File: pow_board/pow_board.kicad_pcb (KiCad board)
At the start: 2 copper layers, 62 x 89.4 mm, 17 parts, among them J1 POWER IN, J2 EXT_USB, J3 EXT_BAT, SW1 SW_SPST, U1 Battery charger module, U2 Step-up DC-DC, U3 Step-down DC-DC

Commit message: Fixed modules sizes
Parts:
- moved U1 0.39 mm to (51.5, 91.6)
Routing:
- net Net-(SW1-B): track 27.5 -> 26.0 mm
- net +BATT: track 87.0 -> 88.5 mm
- net Net-(SW1-A): track 19.5 -> 18.0 mm
- net +5V: track 42.8 -> 43.9 mm
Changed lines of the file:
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@@
 		(at 101.33 82.796 180)
 		(property "Reference" "U2"
-			(at 0.04 13.59 180)
+			(at 16.92 13.56 180)
 			(unlocked yes)
 			(layer "F.SilkS")
@@
 		)
 		(property "Value" "Step-up DC-DC"
-			(at 10.667 22.08 180)
+			(at 16.92 15.06 180)
 			(unlocked yes)
 			(layer "F.Fab")
@@
 		)
 		(property "Footprint" "0a_pow:MT3608_step-up_DC-DC"
-			(at 0.04 14.09 180)
+			(at 16.92 14.06 180)
 			(unlocked yes)
 			(layer "F.Fab")
@@
 		)
 		(property "Datasheet" ""
-			(at 0.04 14.09 180)
+			(at 16.92 14.06 180)
 			(unlocked yes)
 			(layer "F.Fab")
@@
 		)
 		(property "Description" "https://www.mini-tech.com.ua/dc-dc-konverter-povyshayushchij-mt3608"
-			(at 0.04 14.09 180)
+			(at 16.92 14.06 180)
 			(unlocked yes)
 			(layer "F.Fab")
@@
 			)
 		)
-		(sheetname "Root")
-		(sheetfile "pow_board.kicad_sch")
 		(attr through_hole)
 		(fp_rect
-			(start -3.1355 -4.74)
-			(end 34.0755 12.532)
+			(start -3.01 -5.03)
+			(end 32.99 11.97)
 			(stroke
 				(width 0.05)
@@
 			(layer "F.SilkS")
 		)
-		(fp_rect
-			(start -3.1355 -4.74)
-			(end 34.0755 12.532)
-			(stroke
-				(width 0.05)
-				(type default)
-			)
-			(fill none)
-			(layer "F.CrtYd")
-		)
 		(fp_text user "${REFERENCE}"
-			(at 0.04 16.59 180)
+			(at 16.92 16.56 180)
 			(unlocked yes)
 			(layer "F.Fab")
@@
 		)
 		(pad "1" thru_hole rect
-			(at 0 7.87417 180)
+			(at 0 6.5 180)
 			(size 1.7 1.7)
 			(drill 1)
@@
 		)
 		(pad "3" thru_hole rect
-			(at 31.5 0 180)
+			(at 30.5 0 180)
 			(size 1.7 1.7)
 			(drill 1)
@@
 		)
 		(pad "4" thru_hole rect
-			(at 31.5 7.87417 180)
+			(at 30.5 6.5 180)
 			(size 1.7 1.7)
 			(drill 1)
@@
 			(at 4.385 4.81 180)
 			(layer "F.Fab")
+			(hide yes)
 			(effects
 				(font
@@
 			(at 4.385 4.81 0)
 			(layer "F.Fab")
+			(hide yes)
 			(effects
 				(font
@@
 			(at 4.385 12.43 180)
 			(layer "F.Fab")
+			(hide yes)
 			(effects
 				(font
@@
 			(unlocked yes)
 			(layer "F.Fab")
+			(hide yes)
 			(effects
 				(font
@@
 			(at 4.385 4.81 -90)
 			(layer "F.Fab")
+			(hide yes)
 			(effects
 				(font
@@
 	(footprint "0a_pow:TP4056_module_typeC"
 		(layer "F.Cu")
-		(at 51.27 91.3)
+		(at 51.48 91.63)
 		(property "Reference" "U1"
 			(at 0.31 -12.61 0)
@@
 		)
 		(property "Value" "Battery charger module"
-			(at 16.7905 -11.094 0)
+			(at 0.31 -11.11 0)
 			(unlocked yes)
 			(layer "F.Fab")
+			(hide yes)
 			(effects
 				(font
@@
 			)
 		)
-		(sheetname "Root")
-		(sheetfile "pow_board.kicad_sch")
 		(attr through_hole)
 		(fp_rect
-			(start -1.79 3.76)
-			(end 2.67 9.97)
+			(start -2.2 3.755)
+			(end 2.26 9.965)
 			(stroke
 				(width 0.1)
@@
 		)
 		(fp_rect
-			(start -1.21 -1.41)
-			(end 25.79 15.59)
+			(start -1.73 -1.57)
+			(end 26.27 15.63)
 			(stroke
 				(width 0.05)
@@
 			(layer "F.SilkS")
 		)
-		(fp_rect
-			(start -1.21 -1.41)
-			(end 25.79 15.59)
-			(stroke
-				(width 0.05)
-				(type default)
-			)
-			(fill none)
-			(layer "F.CrtYd")
-		)
 		(fp_text user "${REFERENCE}"
 			(at 0.31 -9.61 0)
@@
 		)
 		(pad "3" thru_hole rect
-			(at 22 0)
+			(at 23 0)
 			(size 1.7 1.7)
 			(drill 1)
@@
 		)
 		(pad "4" thru_hole rect
-			(at 22 14)
+			(at 23 14)
 			(size 1.7 1.7)
 			(drill 1)
@@
 		)
 		(pad "5" thru_hole rect
-			(at 22 3)
+			(at 23 2.54)
 			(size 1.7 1.7)
 			(drill 1)
@@
 		)
 		(pad "6" thru_hole rect
-			(at 22 11)
+			(at 23 11.46)
 			(size 1.7 1.7)
 			(drill 1)
@@
 			(at 0 -1.85 180)
 			(layer "B.Fab")
+			(hide yes)
 			(effects
 				(font
@@
 			(at 0.6 -11.3325 90)
 			(layer "B.Fab")
+			(hide yes)
 			(effects
 				(font
@@
 			(at 0 -1.85 180)
 			(layer "B.Fab")
+			(hide yes)
 			(effects
 				(font
@@
 			(at 0 -1.82 0)
 			(layer "B.Fab")
+			(hide yes)
 			(effects
 				(font
@@
 			(at 0 -1.85 -90)
 			(layer "B.Fab")
+			(hide yes)
 			(effects
 				(font
@@
 			(at 0 -1.85 -90)
 			(layer "B.Fab")
+			(hide yes)
 			(effects
 				(font
@@
 	)
 	(gr_text "U"
-		(at 52.33 114.01 180)
+		(at 52.54 114.56 180)
 		(layer "B.Cu")
 		(effects
@@
 	)
 	(gr_text "G"
-		(at 52.32 116.41 180)
+		(at 52.53 116.96 180)
 		(layer "B.Cu")
 		(effects
@@
 	)
 	(segment
-		(start 87.13 62.05)
-		(end 87.13 73.39)
+		(start 56.91 71.51)
+		(end 56.11 71.51)
 		(width 1)
 		(layer "B.Cu")
@@
 	)
 	(segment
-		(start 56.91 71.51)
-		(end 56.11 71.51)
+		(start 86.4 61.41)
+		(end 73.69 61.41)
 		(width 1)
 		(layer "B.Cu")
@@
 	)
 	(segment
-		(start 70.58 94.34)
-		(end 73.12 94.34)
+		(start 59.46 66.27)
+		(end 59.46 71.39)
 		(width 1)
 		(layer "B.Cu")
@@
 	)
 	(segment
-		(start 73.03 94.01)
-		(end 73.05 93.99)
+		(start 59.46 71.39)
+		(end 59.58 71.51)
 		(width 1)
 		(layer "B.Cu")
@@
 	)
 	(segment
-		(start 86.4 61.41)
-		(end 73.69 61.41)
+		(start 87.13 73.39)
+		(end 69.63 90.89)
 		(width 1)
 		(layer "B.Cu")
@@
 	)
 	(segment
-		(start 87.13 73.39)
-		(end 69.63 90.89)
+		(start 73.69 61.41)
+		(end 63.59 71.51)
 		(width 1)
 		(layer "B.Cu")
@@
 	)
 	(segment
-		(start 59.46 66.27)
-		(end 59.46 71.39)
+		(start 69.63 93.39)
+		(end 70.32 94.08)
 		(width 1)
 		(layer "B.Cu")
@@
 	)
 	(segment
-		(start 59.46 71.39)
-		(end 59.58 71.51)
+		(start 55.32 72.3)
+		(end 55.32 75.95)
 		(width 1)
 		(layer "B.Cu")
@@
 	)
 	(segment
-		(start 69.63 93.39)
-		(end 70.58 94.34)
+		(start 63.59 71.51)
+		(end 59.58 71.51)
 		(width 1)
 		(layer "B.Cu")
@@
 	)
 	(segment
-		(start 73.69 61.41)
-		(end 63.59 71.51)
+		(start 55.32 75.95)
+		(end 55.33 75.96)
 		(width 1)
 		(layer "B.Cu")
@@
 	)
 	(segment
-		(start 55.32 72.3)
-		(end 55.32 75.95)
+		(start 70.32 94.08)
+		(end 74.73 94.08)
 		(width 1)
 		(layer "B.Cu")
@@
 	)
 	(segment
-		(start 63.59 71.51)
-		(end 59.58 71.51)
+		(start 87.13 62.05)
+		(end 87.13 73.39)
 		(width 1)
 		(layer "B.Cu")
@@
 	)
 	(segment
-		(start 55.32 75.95)
-		(end 55.33 75.96)
+		(start 59.046 82.796)
+		(end 59.02 82.77)
 		(width 1)
 		(layer "B.Cu")
-		(net 2)
+		(net 3)
 	)
 	(segment
@@
 	)
 	(segment
-		(start 59.046 82.796)
-		(end 59.02 82.77)
+		(start 70.86 82.73)
+		(end 70.794 82.796)
 		(width 1)
 		(layer "B.Cu")
@@
 	)
 	(segment
-		(start 69.83 82.796)
+		(start 70.794 82.796)
 		(end 59.046 82.796)
 		(width 1)
@@
 	)
 	(segment
-		(start 82.29 91.06)
-		(end 73.28 91.06)
+		(start 74.53 91.65)
+		(end 74.46 91.58)
 		(width 1)
 		(layer "B.Cu")
@@
 	)
 	(segment
-		(start 73.28 91.06)
-		(end 73.18 91.16)
+		(start 85.765 94.535)
+		(end 82.88 91.65)
 		(width 1)
 		(layer "B.Cu")
@@
 	)
 	(segment
-		(start 85.765 94.535)
-		(end 82.29 91.06)
+		(start 82.88 91.65)
+		(end 74.53 91.65)
 		(width 1)
 		(layer "B.Cu")
@@
 	)
 	(segment
-		(start 103.37 76.96)
-		(end 103.37 87.89)
+		(start 99.39 91.87)
+		(end 99.39 91.89)
 		(width 1)
 		(layer "B.Cu")
@@
 	)
 	(segment
-		(start 101.3 74.89)
-		(end 103.37 76.96)
+		(start 103.16 78.05)
+		(end 103.16 88.1)
 		(width 1)
 		(layer "B.Cu")
@@
 	)
 	(segment
-		(start 99.39 91.87)
-		(end 99.39 91.89)
+		(start 103.16 88.1)
+		(end 99.39 91.87)
 		(width 1)
 		(layer "B.Cu")
@@
 	)
 	(segment
-		(start 103.37 87.89)
-		(end 99.39 91.87)
+		(start 101.3 76.19)
+		(end 103.16 78.05)
 		(width 1)
 		(layer "B.Cu")

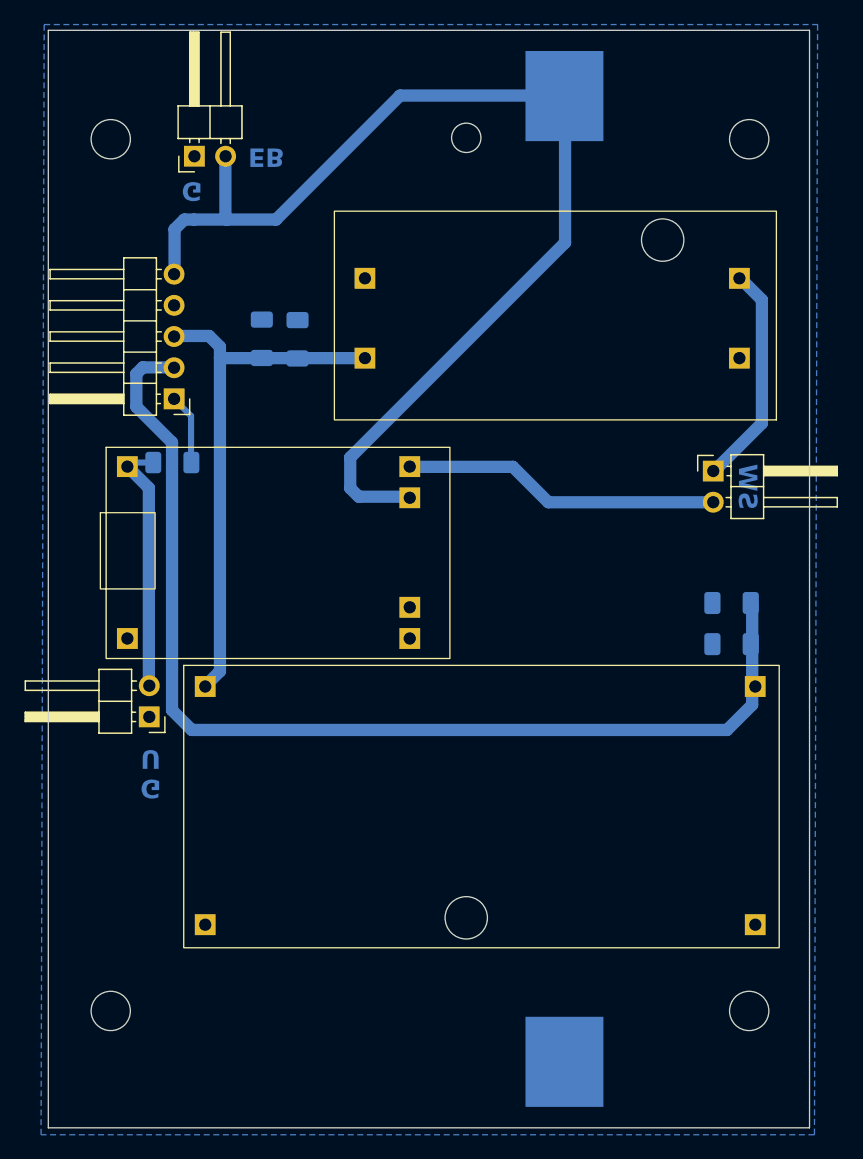
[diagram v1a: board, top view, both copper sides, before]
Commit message: Recovering after git fatal error. Changed M3 to M4
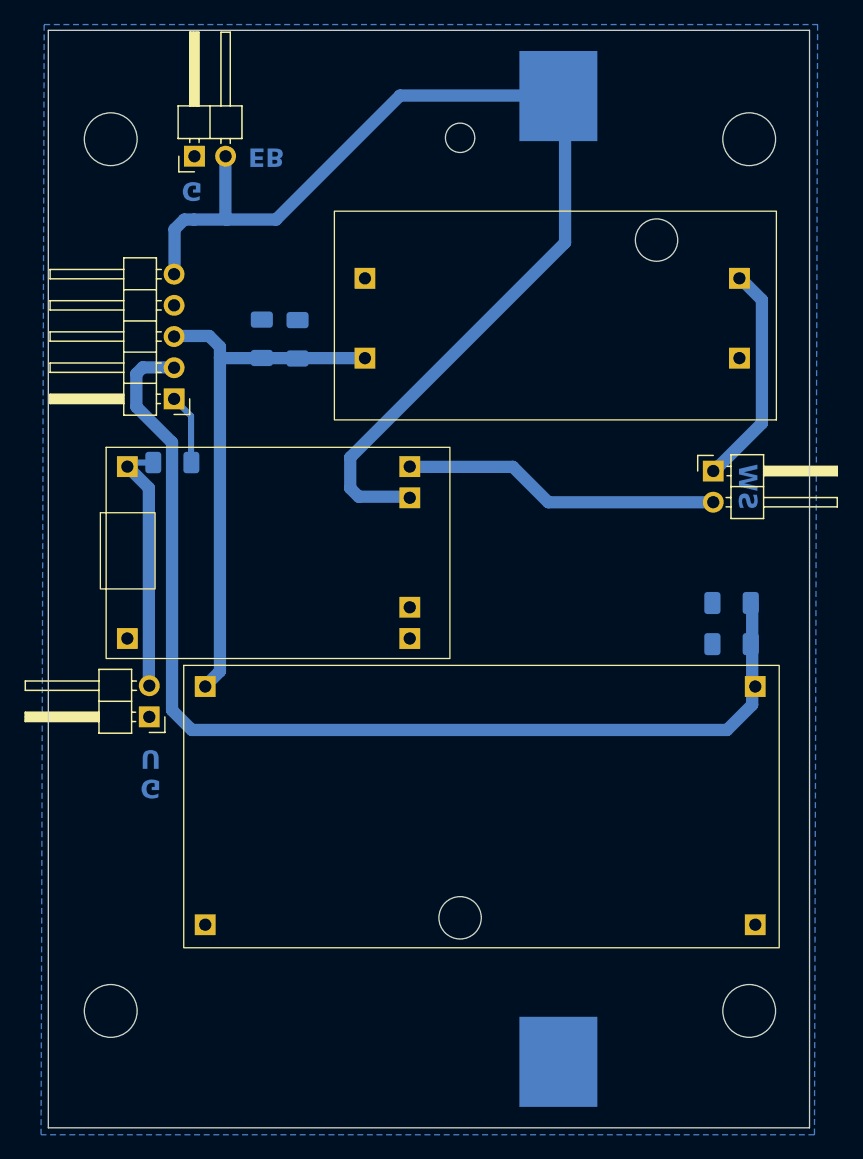
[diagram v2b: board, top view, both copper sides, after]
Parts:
- H1, H2, H3, H4: footprint MountingHole:MountingHole_3.2mm_M3 -> MountingHole:MountingHole_4.3mm_M4
- moved BT1 0.50 mm to (86.6, 100.8)
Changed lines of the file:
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@@
 			)
 		)
+		(sheetname "Root")
+		(sheetfile "pow_board.kicad_sch")
 		(attr through_hole)
 		(fp_rect
@@
 		)
 	)
-	(footprint "MountingHole:MountingHole_3.2mm_M3"
+	(footprint "MountingHole:MountingHole_4.3mm_M4"
 		(layer "F.Cu")
 		(at 50.125 135.965)
-		(descr "Mounting Hole 3.2mm, no annular, M3")
-		(tags "mounting hole 3.2mm no annular m3")
+		(descr "Mounting Hole 4.3mm, no annular, M4")
+		(tags "mounting hole 4.3mm no annular m4")
 		(property "Reference" "H3"
-			(at 0 -4.2 0)
+			(at 0 -5.3 0)
 			(layer "F.SilkS")
 			(hide yes)
@@
 		)
 		(property "Value" "MountingHole"
-			(at 0 4.2 0)
+			(at 0 5.3 0)
 			(layer "F.Fab")
-			(hide yes)
 			(effects
 				(font
@@
 			)
 		)
-		(property "Footprint" "MountingHole:MountingHole_3.2mm_M3"
+		(property "Footprint" "MountingHole:MountingHole_4.3mm_M4"
 			(at 0 0 0)
 			(unlocked yes)
@@
 		(fp_circle
 			(center 0 0)
-			(end 3.2 0)
+			(end 4.3 0)
 			(stroke
 				(width 0.15)
@@
 		(fp_circle
 			(center 0 0)
-			(end 3.45 0)
+			(end 4.55 0)
 			(stroke
 				(width 0.05)
@@
 		(pad "" np_thru_hole circle
 			(at 0 0)
-			(size 3.2 3.2)
-			(drill 3.2)
-			(layers "F&B.Cu" "*.Mask")
+			(size 4.3 4.3)
+			(drill 4.3)
+			(layers "*.Cu" "*.Mask")
 		)
 	)
-	(footprint "MountingHole:MountingHole_3.2mm_M3"
+	(footprint "MountingHole:MountingHole_4.3mm_M4"
 		(layer "F.Cu")
 		(at 102.125 64.965)
-		(descr "Mounting Hole 3.2mm, no annular, M3")
-		(tags "mounting hole 3.2mm no annular m3")
+		(descr "Mounting Hole 4.3mm, no annular, M4")
+		(tags "mounting hole 4.3mm no annular m4")
 		(property "Reference" "H2"
-			(at 0 -4.2 0)
+			(at 0 -5.3 0)
 			(layer "F.SilkS")
 			(hide yes)
@@
 		)
 		(property "Value" "MountingHole"
-			(at 0 4.2 0)
+			(at 0 5.3 0)
 			(layer "F.Fab")
-			(hide yes)
 			(effects
 				(font
@@
 			)
 		)
-		(property "Footprint" "MountingHole:MountingHole_3.2mm_M3"
+		(property "Footprint" "MountingHole:MountingHole_4.3mm_M4"
 			(at 0 0 0)
 			(unlocked yes)
@@
 		(fp_circle
 			(center 0 0)
-			(end 3.2 0)
+			(end 4.3 0)
 			(stroke
 				(width 0.15)
@@
 		(fp_circle
 			(center 0 0)
-			(end 3.45 0)
+			(end 4.55 0)
 			(stroke
 				(width 0.05)
@@
 		(pad "" np_thru_hole circle
 			(at 0 0)
-			(size 3.2 3.2)
-			(drill 3.2)
-			(layers "F&B.Cu" "*.Mask")
+			(size 4.3 4.3)
+			(drill 4.3)
+			(layers "*.Cu" "*.Mask")
 		)
 	)
-	(footprint "MountingHole:MountingHole_3.2mm_M3"
+	(footprint "MountingHole:MountingHole_4.3mm_M4"
 		(layer "F.Cu")
 		(at 50.125 64.965)
-		(descr "Mounting Hole 3.2mm, no annular, M3")
-		(tags "mounting hole 3.2mm no annular m3")
+		(descr "Mounting Hole 4.3mm, no annular, M4")
+		(tags "mounting hole 4.3mm no annular m4")
 		(property "Reference" "H1"
-			(at 0 -4.2 0)
+			(at 0 -5.3 0)
 			(layer "F.SilkS")
 			(hide yes)
@@
 		)
 		(property "Value" "MountingHole"
-			(at 0 4.2 0)
+			(at 0 5.3 0)
 			(layer "F.Fab")
-			(hide yes)
 			(effects
 				(font
@@
 			)
 		)
-		(property "Footprint" "MountingHole:MountingHole_3.2mm_M3"
+		(property "Footprint" "MountingHole:MountingHole_4.3mm_M4"
 			(at 0 0 0)
 			(unlocked yes)
@@
 		(fp_circle
 			(center 0 0)
-			(end 3.2 0)
+			(end 4.3 0)
 			(stroke
 				(width 0.15)
@@
 		(fp_circle
 			(center 0 0)
-			(end 3.45 0)
+			(end 4.55 0)
 			(stroke
 				(width 0.05)
@@
 		(pad "" np_thru_hole circle
 			(at 0 0)
-			(size 3.2 3.2)
-			(drill 3.2)
-			(layers "F&B.Cu" "*.Mask")
+			(size 4.3 4.3)
+			(drill 4.3)
+			(layers "*.Cu" "*.Mask")
 		)
 	)
-	(footprint "MountingHole:MountingHole_3.2mm_M3"
+	(footprint "MountingHole:MountingHole_4.3mm_M4"
 		(layer "F.Cu")
 		(at 102.125 135.965)
-		(descr "Mounting Hole 3.2mm, no annular, M3")
-		(tags "mounting hole 3.2mm no annular m3")
+		(descr "Mounting Hole 4.3mm, no annular, M4")
+		(tags "mounting hole 4.3mm no annular m4")
 		(property "Reference" "H4"
-			(at 0 -4.2 0)
+			(at 0 -5.3 0)
 			(layer "F.SilkS")
 			(hide yes)
@@
 		)
 		(property "Value" "MountingHole"
-			(at 0 4.2 0)
+			(at 0 5.3 0)
 			(layer "F.Fab")
-			(hide yes)
 			(effects
 				(font
@@
 			)
 		)
-		(property "Footprint" "MountingHole:MountingHole_3.2mm_M3"
+		(property "Footprint" "MountingHole:MountingHole_4.3mm_M4"
 			(at 0 0 0)
 			(unlocked yes)
@@
 		(fp_circle
 			(center 0 0)
-			(end 3.2 0)
+			(end 4.3 0)
 			(stroke
 				(width 0.15)
@@
 		(fp_circle
 			(center 0 0)
-			(end 3.45 0)
+			(end 4.55 0)
 			(stroke
 				(width 0.05)
@@
 		(pad "" np_thru_hole circle
 			(at 0 0)
-			(size 3.2 3.2)
-			(drill 3.2)
-			(layers "F&B.Cu" "*.Mask")
+			(size 4.3 4.3)
+			(drill 4.3)
+			(layers "*.Cu" "*.Mask")
 		)
 	)
@@
 			)
 		)
+		(sheetname "Root")
+		(sheetfile "pow_board.kicad_sch")
 		(attr through_hole)
 		(fp_rect
@@
 	(footprint "Battery:BatteryHolder_Keystone_1042_1x18650"
 		(layer "B.Cu")
-		(at 87.08 100.78 -90)
+		(at 86.58 100.78 -90)
 		(descr "Battery holder for 18650 cylindrical cells http://www.keyelco.com/product.cfm/product_id/918")
 		(tags "18650 Keystone 1042 Li-ion")

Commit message: Update
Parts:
- added D1: VS-15MQ040NTRPBF, Diode_SMD:D_SMA_Handsoldering, B.Cu at (99.2, 101.0)
- added Q1: IRLML6401, Package_TO_SOT_SMD:SOT-23, B.Cu at (102.9, 101.0)
- added R2: 10k, Resistor_SMD:R_1206_3216Metric_Pad1.30x1.75mm_HandSolder, B.Cu at (103.5, 104.4)
- added R3: 0R, Resistor_SMD:R_1206_3216Metric_Pad1.30x1.75mm_HandSolder, B.Cu at (70.7, 113.1)
- added R4: 0R, Resistor_SMD:R_1206_3216Metric_Pad1.30x1.75mm_HandSolder, B.Cu at (59.1, 94.5)
- added R5: 0R, Resistor_SMD:R_1206_3216Metric_Pad1.30x1.75mm_HandSolder, B.Cu at (70.7, 119.7)
- added R6: 0R, Resistor_SMD:R_1206_3216Metric_Pad1.30x1.75mm_HandSolder, B.Cu at (73.8, 113.1)
- moved C4 16.3 mm to (100.8, 119.0), turned to 0 degrees
- moved C5 9.58 mm to (100.8, 115.7), turned to 0 degrees
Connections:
- BT1 pad 2: GND -> -BATT
- SW1 pad 2: Net-(SW1-B) -> Net-(D1-K)
- U1 pad 3: Net-(SW1-B) -> +BATT
- U1 pad 6: GND -> -BATT
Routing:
- net -BATT: track 0.00 -> 47.9 mm
- net VBUS: track 27.0 -> 73.0 mm
- net +BATT: track 88.5 -> 128.0 mm
- net Net-(SW1-B): track 26.0 -> 0.00 mm
- net Net-(D1-K): track 0.00 -> 7.80 mm
- net +3.3V: track 89.0 -> 88.4 mm
- added copper zone on B.Cu, net VBUS
